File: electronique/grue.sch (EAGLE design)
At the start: 23 parts, among them IC3 REG1117, Q1 BSS138, Q2 BSS138

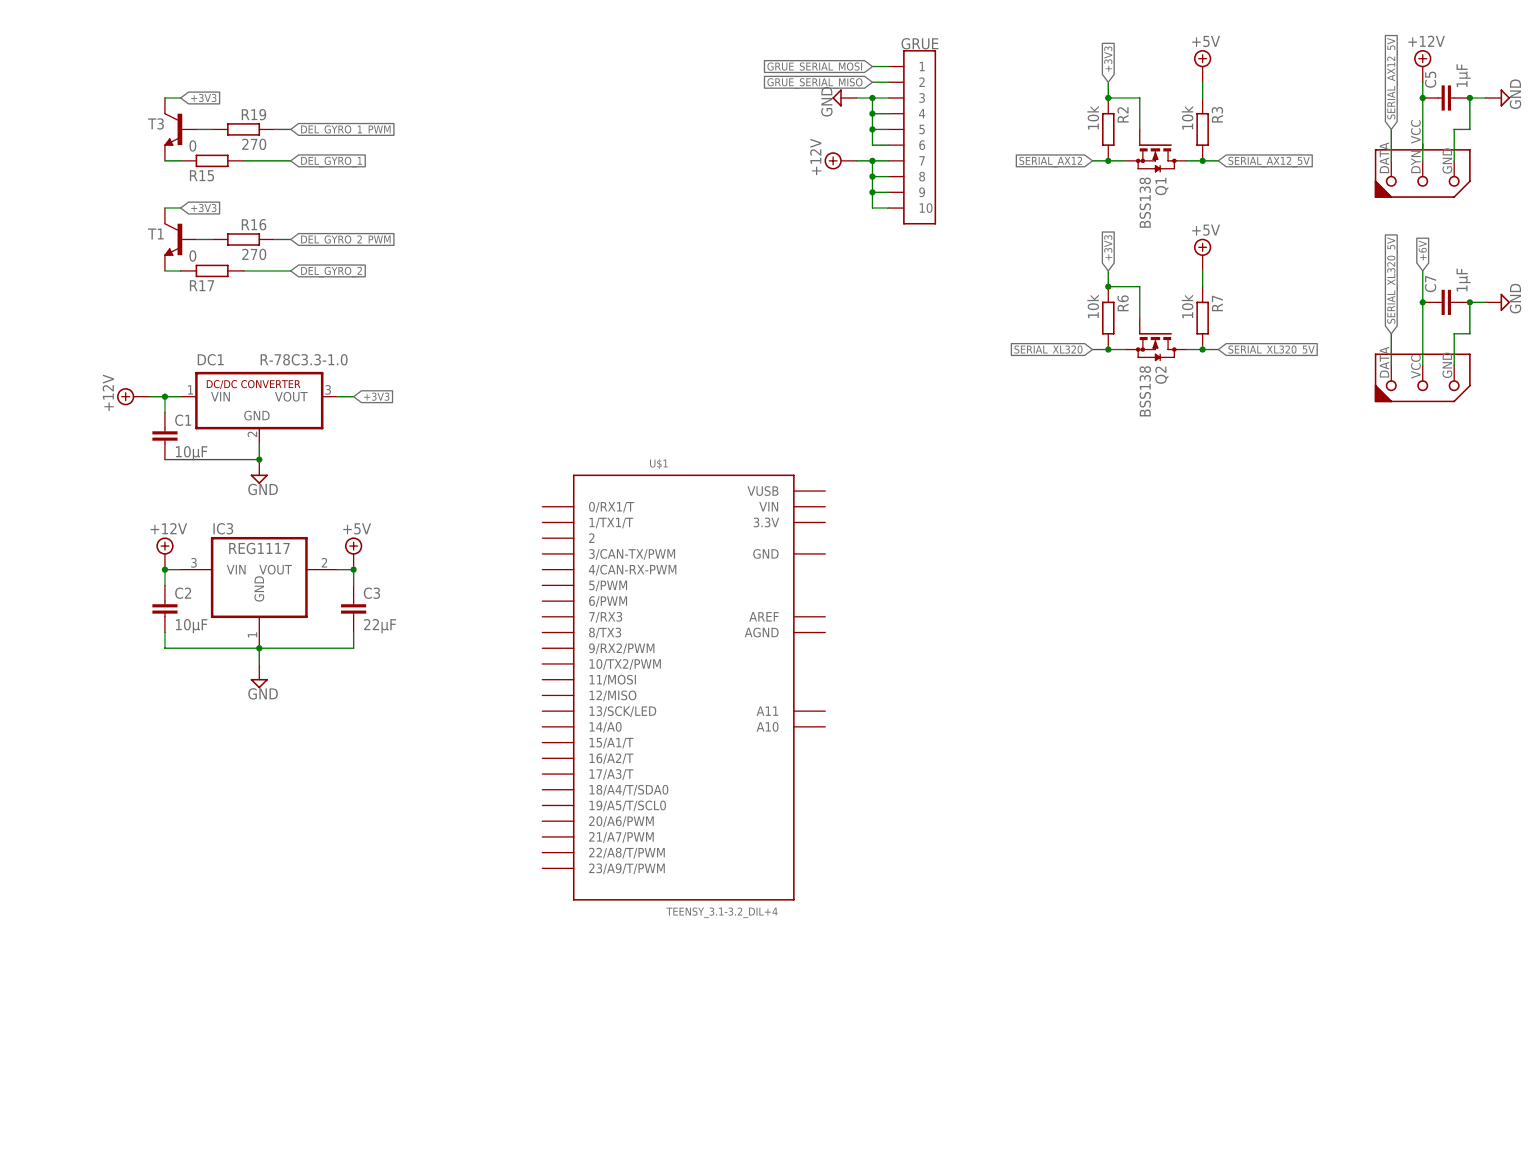
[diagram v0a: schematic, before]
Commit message: Ajout lib Eagle DC-DC-converter
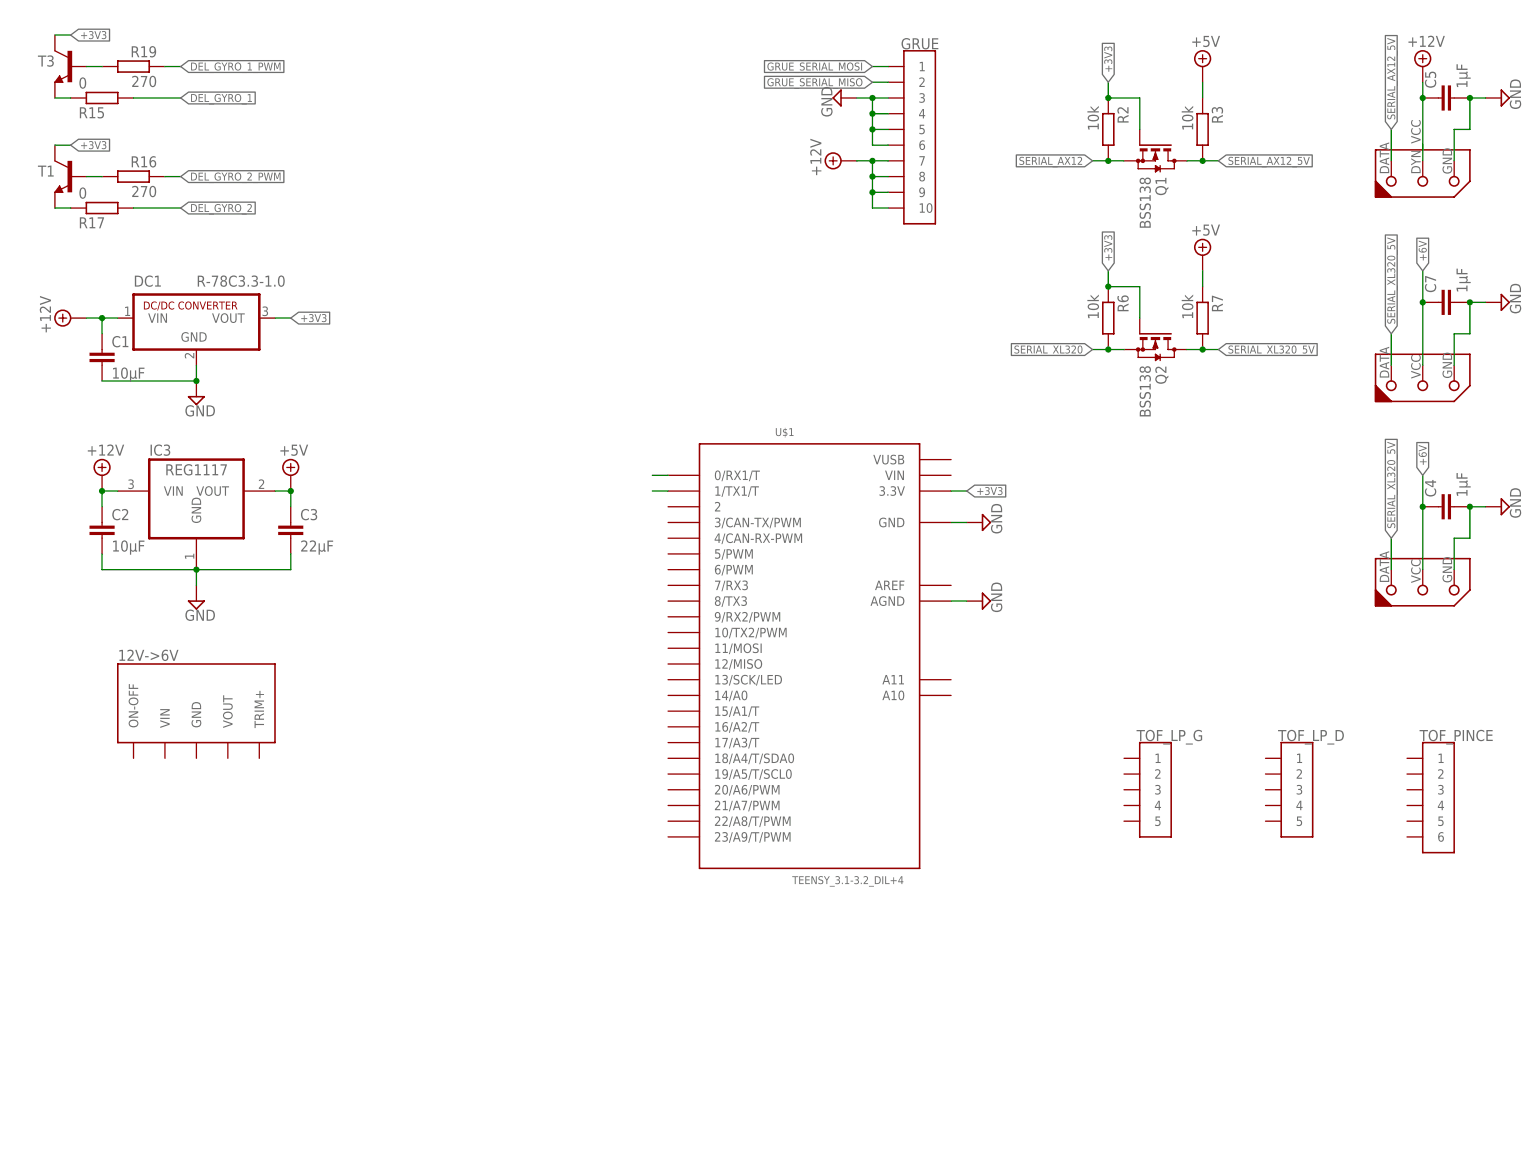
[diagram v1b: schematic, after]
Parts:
- added 12V->6V: DC-DC-CONVERTER, dc-dc-converter:DC-DC-CONVERTER
- added C4: 1µF, resistor:C-EUC0805
- added TOF_LP_D, TOF_LP_G: JST-05, con-jst:JST-05
- added TOF_PINCE: JST-06, con-jst:JST-06
- added XL320_G1: DYNAMIXEL-1X03XL, 1NTech_pinhead:DYNAMIXEL-1X03XL
- IC3: RS (none) -> 885-5432
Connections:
- new net N$1: U$1.0/RX1/T
- new net N$2: U$1.1/TX1/T
- net +3V3: now also U$1.3.3V
- net +6V: now also C4.1, XL320_G1.DYN_VCC
- net GND: now also C4.2, U$1.AGND, U$1.GND, XL320_G1.GND
- net SERIAL_XL320_5V: now also XL320_G1.DATA
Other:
- moved on the sheet: C1, C2, C3, DC1, IC3, R15, R16, R17, R19, T1, T3, U$1

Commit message: Carte secondaire : schéma presque fini, il manque juste 2 pins à la teensy... :'(
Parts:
- removed 12V->6V: DC-DC-CONVERTER, dc-dc-converter:DC-DC-CONVERTER
- removed TOF_LP_D: JST-05, con-jst:JST-05
- added C6: 1µF, resistor:C-EUC0805
- added DC-DC-6V: DC-DC-CONVERTER, dc-dc-converter-6v:DC-DC-CONVERTER
- added GYRO: JST-04GH-V, con-jst:JST-04GH-V
- added MOT_H, MOT_V: (no value), pinhead:PINHD-1X6
- added R1: 220, resistor:R-EU_R0805
- added R10, R4, R5, R8, R9: 10k, resistor:R-EU_R0805
- added TOF_LP_D_AND_DISPLAY: JST-05, con-jst:JST-05
- added U$2, U$3, U$4, U$5, U$6: PUSH-BUTTON, push-button:PUSH-BUTTON
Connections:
- removed net N$2: U$1.1/TX1/T
- new net ENABLE: R1.1
- new net INPUT1: R2.1
- new net INPUT2: R3.1
- new net MOT_H_EN: U$1.3/CAN-TX/PWM
- new net MOT_H_ENC_A: MOT_H.5
- new net MOT_H_ENC_B: MOT_H.6
- new net MOT_H_IN1: U$1.4/CAN-RX-PWM
- new net MOT_H_IN2: U$1.5/PWM
- new net MOT_H_OUT+: MOT_H.1
- new net MOT_H_OUT-: MOT_H.2
- new net MOT_V_EN: U$1.21/A7/PWM
- new net MOT_V_ENC_A: MOT_V.5
- new net MOT_V_ENC_B: MOT_V.6
- new net MOT_V_IN1: U$1.22/A8/T/PWM
- new net MOT_V_IN2: U$1.23/A9/T/PWM
- new net MOT_V_OUT+: MOT_V.1
- new net MOT_V_OUT-: MOT_V.2
- new net N$13: R5.2, U$1.13/SCK/LED, U$2.P$2
- new net N$14: R8.2, U$1.14/A0, U$3.P$2
- new net N$15: R9.1, U$1.15/A1/T, U$4.P$2
- new net N$16: R10.1, U$1.16/A2/T, U$5.P$2
- new net N$3: DC-DC-6V.TRIM+, R1.2
- new net SCL: TOF_LP_D_AND_DISPLAY.4, TOF_LP_G.4, TOF_PINCE.4, U$1.19/A5/T/SCL0
- new net SDA: TOF_LP_D_AND_DISPLAY.3, TOF_LP_G.3, TOF_PINCE.3, U$1.18/A4/T/SDA0
- new net TOF_LP_D: TOF_LP_D_AND_DISPLAY.5, U$1.11/MOSI
- new net TOF_LP_G: TOF_LP_G.5, U$1.2
- new net TOF_PINCE_EXT: TOF_PINCE.6, U$1.17/A3/T
- new net TOF_PINCE_INT: TOF_PINCE.5, U$1.12/MISO
- net +12V: now also C1.2, DC-DC-6V.VIN
- net +3V3: now also R10.2, R4.2, R5.1, R8.1, R9.2, TOF_LP_D_AND_DISPLAY.2, TOF_LP_G.2, TOF_PINCE.2
- net +5V: now also C2.2, MOT_H.4, MOT_V.4
- net +6V: now also DC-DC-6V.VOUT
- net DEL_GYRO_1: now also GYRO.1
- net DEL_GYRO_1_PWM: now also U$1.6/PWM
- net DEL_GYRO_2: now also GYRO.3
- net DEL_GYRO_2_PWM: now also U$1.20/A6/PWM
- net GND: now also C1.1, C2.1, C6.1, DC-DC-6V.GND, GYRO.2, GYRO.4, MOT_H.3, MOT_V.3, R1.1, R1.2, R2.2, R3.2, TOF_LP_D_AND_DISPLAY.1, TOF_LP_G.1, TOF_PINCE.1, U$2.P$1, U$3.P$1, U$4.P$1, U$5.P$1, U$6.P$2
- net GRUE_SERIAL_MISO: now also U$1.1/TX1/T
- net GRUE_SERIAL_MOSI: now also U$1.0/RX1/T
- net N$1: now also C6.2, R4.1, U$1.A10, U$6.P$1; no longer U$1.0/RX1/T
- net SERIAL_AX12: now also U$1.10/TX2/PWM, U$1.9/RX2/PWM
- net SERIAL_XL320: now also U$1.7/RX3, U$1.8/TX3
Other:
- moved on the sheet: C1, C2, C3, DC1, IC3, TOF_LP_G, TOF_PINCE, U$1

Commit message: Comment ça il n'y a plus de pins dispo ? mais enfin tout va bien !
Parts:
- removed C6: 1µF, resistor:C-EUC0805
- removed R10, R4, R5, R8, R9: 10k, resistor:R-EU_R0805
- removed U$2, U$3, U$4, U$5, U$6: PUSH-BUTTON, push-button:PUSH-BUTTON
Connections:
- removed net N$13: R5.2, U$1.13/SCK/LED, U$2.P$2
- removed net N$14: R8.2, U$1.14/A0, U$3.P$2
- removed net N$15: R9.1, U$1.15/A1/T, U$4.P$2
- removed net N$16: R10.1, U$1.16/A2/T, U$5.P$2
- new net ADC: C1.2, R1.2
- new net LOGIC_HIGH: R1.1
- new net LOGIC_LOW: C1.1, R2.2, R3.2
- new net N$2: U$1.A11
- new net N$4: R3.1
- net +3V3: no longer R10.2, R4.2, R5.1, R8.1, R9.2
- net GND: no longer C6.1, U$2.P$1, U$3.P$1, U$4.P$1, U$5.P$1, U$6.P$2
- net MOT_H_ENC_A: now also U$1.11/MOSI
- net MOT_H_ENC_B: now also U$1.12/MISO
- net MOT_V_ENC_A: now also U$1.15/A1/T
- net MOT_V_ENC_B: now also U$1.16/A2/T
- net N$1: no longer C6.2, R4.1, U$6.P$1
- net N$3: now also R2.1
- net TOF_LP_D: now also U$1.13/SCK/LED; no longer U$1.11/MOSI
- net TOF_PINCE_INT: now also U$1.14/A0; no longer U$1.12/MISO
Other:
- moved on the sheet: DC-DC-6V, R1, TOF_LP_D_AND_DISPLAY, TOF_LP_G, TOF_PINCE, U$1

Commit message: L'élec ça c'est fait !
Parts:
- added F1: MF-LSMF300, polyswitch:MF-LSMF300
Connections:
- net ENABLE renamed ENABLE_A
- removed net INPUT2: R3.1
- new net ENABLE_B: R2.1
- new net INPUT4: R6.1
- net +6V: now also F1.2
- net GND: now also R6.2
- net INPUT1: now also R3.1; no longer R2.1
- net N$4: now also F1.1
